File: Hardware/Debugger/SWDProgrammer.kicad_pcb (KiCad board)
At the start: 4 copper layers, 24.5 x 30.1 mm, 40 parts, among them J1 USB_C_Receptacle_USB2.0, J2 USB_C_Receptacle_USB2.0, U1 AP2112K-3.3, U2 STM32F103C8Tx, Y1 32.768KHZ, Y2 8Mhz

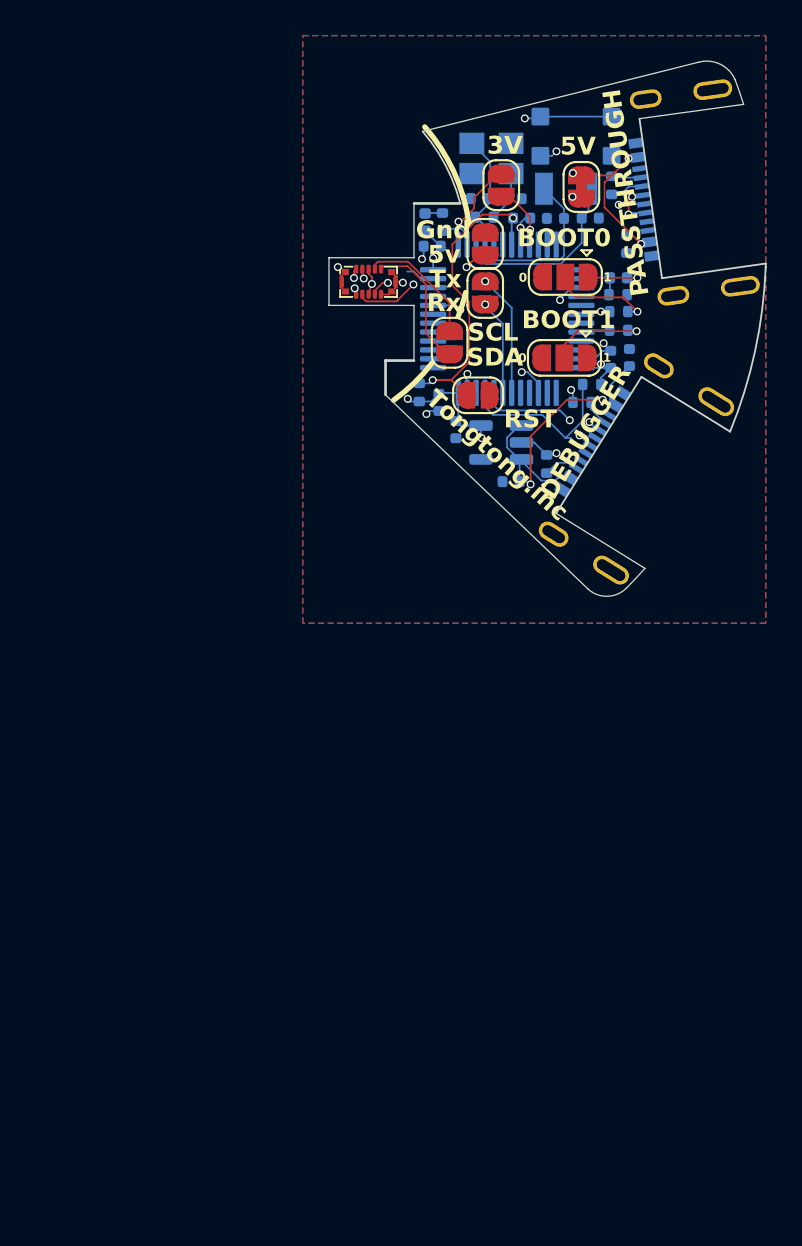
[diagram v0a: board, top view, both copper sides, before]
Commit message: added ID column
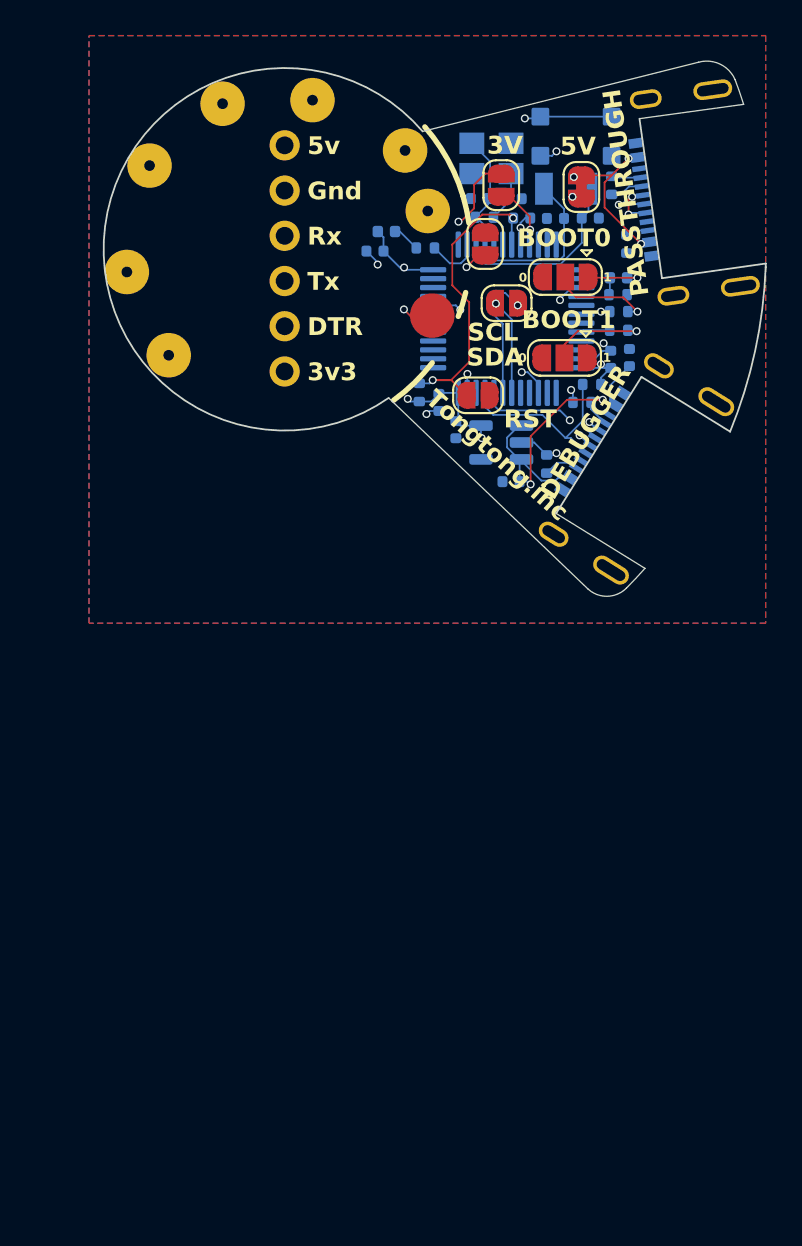
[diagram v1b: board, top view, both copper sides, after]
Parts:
- removed the JP7 at (139.2, 65.2)
- removed U3: ~, Library:BK13C06-10DP
- added ?: , , F.Cu at (130.0, 66.9)
- added ?: , , F.Cu at (130.0, 56.7)
- added ?: , , F.Cu at (122.4, 55.3)
- added ?: , , F.Cu at (130.0, 59.2)
- added ?: , , F.Cu at (131.6, 51.6)
- added ?: , , F.Cu at (123.5, 66.0)
- added ?: , , F.Cu at (130.0, 54.2)
- added ?: , , F.Cu at (138.0, 57.9)
- added ?: , , F.Cu at (130.0, 61.8)
- added ?: , , F.Cu at (136.8, 54.5)
- added ?: , , F.Cu at (126.5, 51.8)
- added ?: , , F.Cu at (130.0, 64.3)
- added ?: , , F.Cu at (138.3, 63.7)
- added ?: , , F.Cu at (121.1, 61.3)
- D1: value BLUE -> White
- S1: value Button 3x3x1.5 -> Button
- moved C7 3.23 mm to (135.1, 60.1)
- moved D1 2.24 mm to (135.7, 59.0), turned to 180 degrees
- moved R3 1.74 mm to (137.9, 59.9), turned to 0 degrees
- moved JP7 1.33 mm to (142.4, 63.0), turned to 180 degrees
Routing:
- net /A10: track 5.37 -> 25.9 mm
- net 5V: track 41.6 -> 59.7 mm
- net /A9: track 6.88 -> 20.0 mm
- net swc: track 14.9 -> 26.9 mm, vias 2 -> 1
- net swd: track 13.9 -> 22.1 mm, vias 2 -> 1
- net SDA: track 7.58 -> 0.00 mm
- net RESET: track 19.8 -> 12.6 mm, vias 2 -> 1
- net SCL: track 7.05 -> 0.00 mm
- net VDD_nRF: track 14.4 -> 21.4 mm, vias 2 -> 1
- net D+: track 21.6 -> 17.0 mm, vias 3 -> 2
- net GND: track 14.9 -> 11.2 mm, vias 9 -> 8
- net 3.3V: track 21.1 -> 22.8 mm
- net D-: track 22.0 -> 23.3 mm, vias 2 -> 1
- net 5V(2): track 24.9 -> 23.8 mm
- net /PC13: track 2.14 -> 3.04 mm
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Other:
- board size 24.5 x 30.1 mm -> 37.2 x 30.1 mm
- board text added: "3v3"
- board text added: "DTR"

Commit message: new debugger
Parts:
- removed ? (x14): , 
- removed JP7 (x2): SolderJumper_2_Open, Jumper:SolderJumper-2_P1.3mm_Open_RoundedPad1.0x1.5mm
- added U4: Conn_01x14_Socket, Library:FPC, F.Cu at (136.5, 100.1)
- C1, C10, C11, C2, C3, C4, C5, C6, C7, C8, C9, D1, D2, J1, J2, R1, R10, R11, R12, R13, R2, R3, R4, R7, R8, R9, U1, U2, Y1, Y2: moved to F.Cu
- JP4, JP5: moved to B.Cu
- S1: value Button -> Button 3*3*1.5; moved to F.Cu
- moved J2 57.1 mm to (121.8, 106.5), turned to 90 degrees
- moved R12 55.8 mm to (123.2, 109.1)
- moved Y1 54.4 mm to (130.0, 108.7), turned to 180 degrees
- moved R13 54.2 mm to (123.3, 104.5), turned to -90 degrees
- moved Y2 51.9 mm to (133.3, 106.1), turned to 45 degrees
- moved C3 51.6 mm to (129.9, 106.9)
- moved C11 51.0 mm to (134.9, 107.7), turned to -135 degrees
- moved JP2 50.7 mm to (124.9, 107.7), turned to 90 degrees
- moved JP5 49.7 mm to (134.6, 104.8), turned to 45 degrees
- moved C4 49.2 mm to (130.9, 105.3), turned to -135 degrees
- moved D1 48.6 mm to (128.0, 106.9)
- moved C10 48.1 mm to (135.7, 104.7), turned to 135 degrees
- moved R1 47.5 mm to (124.8, 104.5), turned to 135 degrees
- moved C9 47.3 mm to (127.1, 108.5), turned to 180 degrees
- moved R3 47.0 mm to (128.2, 105.9)
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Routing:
- net 5V: track 59.7 -> 25.5 mm, vias 4 -> 5
- net /A10: track 25.9 -> 0.00 mm, vias 1 -> 0
- net /A9: track 20.0 -> 0.00 mm, vias 1 -> 0
- net swc: track 26.9 -> 7.86 mm, vias 1 -> 2
- net VDD_nRF: track 21.4 -> 2.64 mm
- net swd: track 22.1 -> 10.1 mm, vias 1 -> 2
- net Net-(U2-BOOT0): track 10.8 -> 1.67 mm, vias 2 -> 0
- net 3.3V: track 22.8 -> 14.6 mm, vias 6 -> 10
- net Net-(JP1-A): track 18.3 -> 11.4 mm, vias 2 -> 0
- net Net-(U2-PC14): track 10.4 -> 5.31 mm
- net Net-(U2-PC15): track 9.46 -> 5.56 mm
- net Batteryin: track 0.00 -> 3.30 mm, vias 0 -> 1
- net RESET: track 12.6 -> 15.6 mm, vias 1 -> 2
- net D-: track 23.3 -> 20.5 mm, vias 1 -> 3
- net /BOOT0: track 6.30 -> 3.61 mm, vias 1 -> 0
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- added copper zone on In2.Cu, net 5V
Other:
- board size 37.2 x 30.1 mm -> 23.2 x 27 mm
- board text removed: "0"
- board text removed: "1"
- board text removed: "3V"
- board text removed: "3v3"
- board text removed: "5V"
- board text removed: "5v"
- board text removed: "BOOT0"
- board text removed: "BOOT1"
- board text removed: "DEBUGGER"
- board text removed: "DTR"
- board text removed: "Gnd"
- board text removed: "PASSTHROUGH"
- board text removed: "RST"
- board text removed: "Rx"
- board text removed: "SCL"
- board text removed: "SDA"
- board text removed: "Tongtong.inc"
- board text removed: "Tx"

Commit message: current version
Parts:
- added REF**: PinHeader_1x04_P1.00mm_Vertical, Connector_PinHeader_1.00mm:PinHeader_1x04_P1.00mm_Vertical, B.Cu at (128.8, 98.0)
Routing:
- net 5V: track 25.5 -> 30.8 mm
- net /A9: track 0.00 -> 3.26 mm
- net /A10: track 0.00 -> 3.14 mm
- net GND: track 9.34 -> 8.46 mm
- net 3.3V: track 14.6 -> 15.4 mm
- net 5V(2): track 26.4 -> 25.7 mm
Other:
- board text added: "5V"
- board text added: "Debugger"
- board text added: "GND"
- board text added: "Passthrough"
- board text added: "RX"
- board text added: "TX"

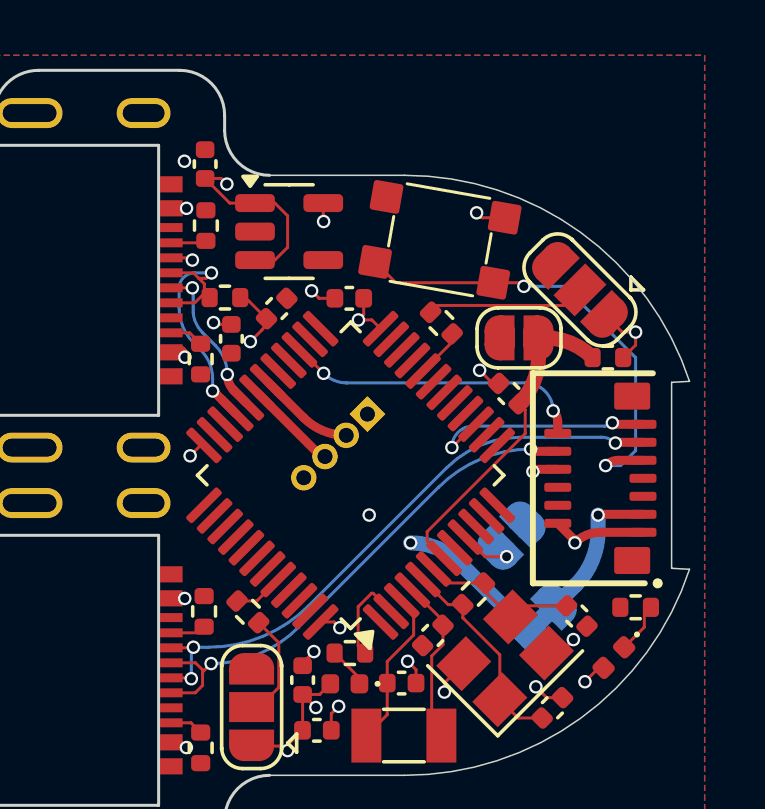
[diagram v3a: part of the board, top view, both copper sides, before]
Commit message: added gyro, flex pcb antenna
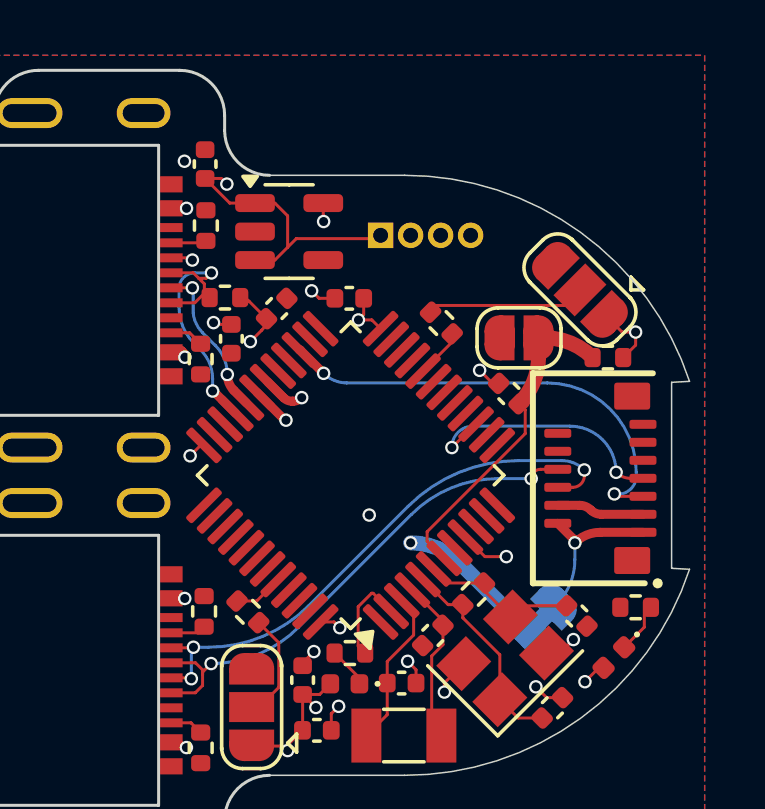
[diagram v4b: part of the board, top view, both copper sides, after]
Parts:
- removed JP4: Jumper_2_Open, Jumper:SolderJumper-2_P1.3mm_Open_RoundedPad1.0x1.5mm
- removed S1: Button 3*3*1.5, Library:button 3x3
- moved REF** 5.98 mm to (129.2, 92.0), turned to -90 degrees
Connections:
- U4 pad 1: Batteryin -> 5V(2)
- U4 pad 10: D+ -> GND
- U4 pad 11: D- -> antenna
- U4 pad 12: swd -> GND
- U4 pad 13: swc -> GND
- U4 pad 2: Batteryin -> 5V(2)
- U4 pad 3: 5V(2) -> Batteryin
- U4 pad 4: GND -> Batteryin
- U4 pad 5: GND -> swd
- U4 pad 6: SCL -> D-
- U4 pad 7: SDA -> swc
- U4 pad 8: VDD_nRF -> D+
- U4 pad 9: RESET -> GND
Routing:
- net RESET: track 15.6 -> 0.00 mm, vias 2 -> 0
- net /A10: track 3.14 -> 11.2 mm, vias 0 -> 1
- net /A9: track 3.26 -> 9.35 mm, vias 0 -> 1
- net swd: track 10.1 -> 15.4 mm
- net 5V: track 30.8 -> 34.1 mm
- net VDD_nRF: track 2.64 -> 0.00 mm, vias 1 -> 0
- net D-: track 20.1 -> 19.0 mm
- net GND: track 8.46 -> 7.45 mm, vias 10 -> 9
- net swc: track 7.93 -> 8.75 mm
- net Batteryin: track 3.23 -> 2.92 mm, vias 1 -> 0

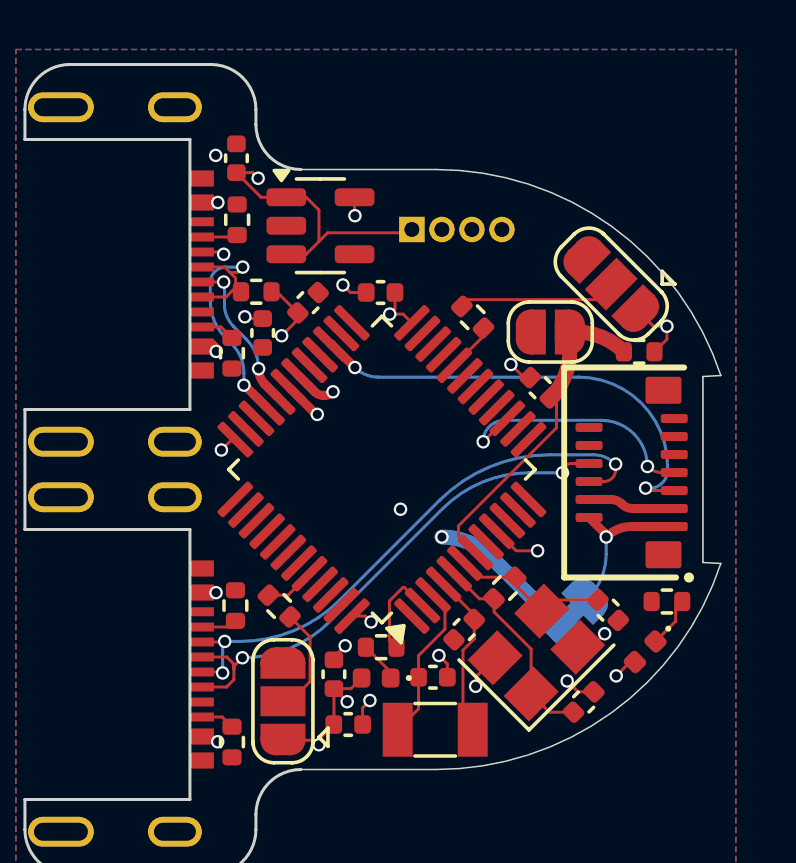
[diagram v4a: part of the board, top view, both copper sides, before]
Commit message: revolute production boards
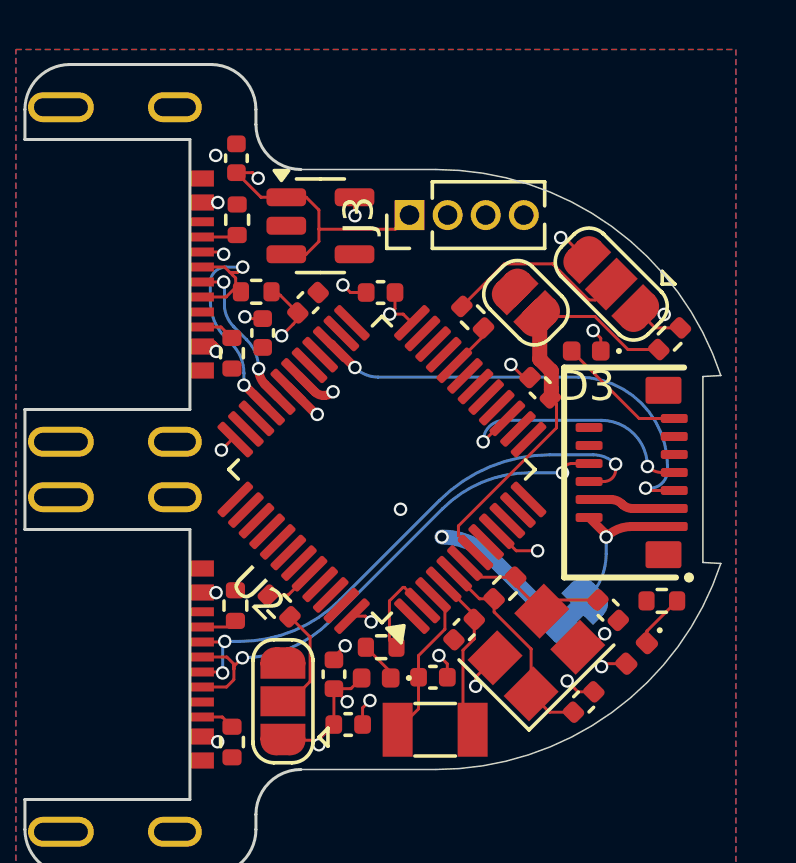
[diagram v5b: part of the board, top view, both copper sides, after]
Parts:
- removed REF**: PinHeader_1x04_P1.00mm_Vertical, Connector_PinHeader_1.00mm:PinHeader_1x04_P1.00mm_Vertical
- added D3: White, LED_SMD:LED_0402_1005Metric, F.Cu at (135.0, 96.0)
- added J3: Conn_01x04_Pin, Connector_PinHeader_1.27mm:PinHeader_1x04_P1.27mm_Vertical, F.Cu at (129.1, 91.5)
- U2: value STM32F103C8Tx -> STM32F103CBTx
- moved JP1 1.27 mm to (133.0, 94.4), turned to 135 degrees
- moved R4 1.10 mm to (137.8, 95.6), turned to -135 degrees
- moved D2 0.29 mm to (136.7, 106.1)
- moved R8 0.17 mm to (137.5, 104.4)
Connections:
- U2 pad 30: /A9 -> /TX
- U2 pad 31: /A10 -> /RX
- U4 pad 13: GND -> led
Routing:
- net /RX: track 0.00 -> 11.9 mm, vias 0 -> 1
- net /A10: track 11.2 -> 0.00 mm, vias 1 -> 0
- net /TX: track 0.00 -> 9.91 mm, vias 0 -> 1
- net /A9: track 9.35 -> 0.00 mm, vias 1 -> 0
- net led: track 0.00 -> 4.35 mm
- net Net-(JP1-A): track 11.2 -> 14.1 mm
- net GND: track 7.45 -> 9.26 mm, vias 9 -> 11
- net /BOOT1: track 5.29 -> 6.29 mm
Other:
- board text added: "BOOT0"
- board text added: "BOOT1"
- board text added: "G"
- board text removed: "GND"
